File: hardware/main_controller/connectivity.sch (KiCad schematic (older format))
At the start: 16 parts

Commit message: Peripherals
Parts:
- removed JP?: Jumper, symbol Device:Jumper
- added J? (x2): Conn_01x08, symbol Connector_Generic:Conn_01x08
- added J? (x2): Conn_02x08_Odd_Even, symbol Connector_Generic:Conn_02x08_Odd_Even
- added J?: Conn_01x04, symbol Connector_Generic:Conn_01x04
- added J?: Conn_01x06, symbol Connector_Generic:Conn_01x06
- added J?: Conn_02x03_Counter_Clockwise, symbol Connector_Generic:Conn_02x03_Counter_Clockwise
- added J? (x2): RJ45, symbol Connector:RJ45
- added JP? (x3): Jumper_NO_Small, symbol Device:Jumper_NO_Small
- added R?: 4.7k, symbol Device:R
- added R?: 120, symbol Device:R
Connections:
- net labels added: CAN_H, CAN_L, CAN_PWR, CAN_RX, CAN_TX, GPIO_PE0, GPIO_PE1, GPIO_PE10, GPIO_PE11, GPIO_PE12, GPIO_PE13, GPIO_PE14, GPIO_PE15, GPIO_PE2, GPIO_PE3, GPIO_PE4, GPIO_PE5, GPIO_PE6, GPIO_PE7, GPIO_PE8, GPIO_PE9, I2C_SCL, I2C_SDA, SPI_CS1, SPI_CS2, SPI_CS3, SPI_MISO, SPI_MOSI, SPI_SCK
- wire segments 71 -> 219
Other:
- note added: "CAN"
- note added: "Deliver/Retrieve Power from CAN bus"
- note added: "GPIO"
- note added: "I2C"
- note added: "Optional CAN bus\ntermination resistor"
- note added: "SPI"
- moved on the sheet: C?, U?

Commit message: LEDs
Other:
- moved on the sheet: J?
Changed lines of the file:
@@
 L Connector_Generic:Conn_01x06 J?
 U 1 1 5FF94D26
-P 4650 4050
-F 0 "J?" H 4568 3525 50  0000 C CNN
-F 1 "Conn_01x06" H 4568 3616 50  0000 C CNN
-F 2 "" H 4650 4050 50  0001 C CNN
-F 3 "~" H 4650 4050 50  0001 C CNN
-	1    4650 4050
+P 4650 4200
+F 0 "J?" H 4568 3675 50  0000 C CNN
+F 1 "Conn_01x06" H 4568 3766 50  0000 C CNN
+F 2 "" H 4650 4200 50  0001 C CNN
+F 3 "~" H 4650 4200 50  0001 C CNN
+	1    4650 4200
 	-1   0    0    1
 $EndComp
 Wire Wire Line
-	4850 3750 4950 3750
-Wire Wire Line
-	4850 3850 4950 3850
-Wire Wire Line
-	4850 3950 4950 3950
-Wire Wire Line
-	4850 4050 4950 4050
-Wire Wire Line
-	4850 4150 4950 4150
-Wire Wire Line
-	4850 4250 4950 4250
-Text GLabel 4950 3750 2    50   Input ~ 0
+	4850 3900 4950 3900
+Wire Wire Line
+	4850 4000 4950 4000
+Wire Wire Line
+	4850 4100 4950 4100
+Wire Wire Line
+	4850 4200 4950 4200
+Wire Wire Line
+	4850 4300 4950 4300
+Wire Wire Line
+	4850 4400 4950 4400
+Text GLabel 4950 3900 2    50   Input ~ 0
 SPI_SCK
-Text GLabel 4950 3850 2    50   Input ~ 0
+Text GLabel 4950 4000 2    50   Input ~ 0
 SPI_MISO
-Text GLabel 4950 3950 2    50   Input ~ 0
+Text GLabel 4950 4100 2    50   Input ~ 0
 SPI_MOSI
-Text GLabel 4950 4050 2    50   Input ~ 0
+Text GLabel 4950 4200 2    50   Input ~ 0
 SPI_CS1
-Text GLabel 4950 4150 2    50   Input ~ 0
+Text GLabel 4950 4300 2    50   Input ~ 0
 SPI_CS2
-Text GLabel 4950 4250 2    50   Input ~ 0
+Text GLabel 4950 4400 2    50   Input ~ 0
 SPI_CS3
 $Comp
 L Connector_Generic:Conn_02x03_Counter_Clockwise J?
 U 1 1 5FFE4E2A
-P 4850 4900
-F 0 "J?" H 4900 5217 50  0000 C CNN
-F 1 "Conn_02x03_Counter_Clockwise" H 4900 5126 50  0000 C CNN
-F 2 "" H 4850 4900 50  0001 C CNN
-F 3 "~" H 4850 4900 50  0001 C CNN
-	1    4850 4900
+P 4850 5050
+F 0 "J?" H 4900 5367 50  0000 C CNN
+F 1 "Conn_02x03_Counter_Clockwise" H 4900 5276 50  0000 C CNN
+F 2 "" H 4850 5050 50  0001 C CNN
+F 3 "~" H 4850 5050 50  0001 C CNN
+	1    4850 5050
 	1    0    0    -1
 $EndComp
@@
 L power:+3V3 #PWR?
 U 1 1 5FFE6348
-P 4600 4650
-F 0 "#PWR?" H 4600 4500 50  0001 C CNN
-F 1 "+3V3" H 4615 4823 50  0000 C CNN
-F 2 "" H 4600 4650 50  0001 C CNN
-F 3 "" H 4600 4650 50  0001 C CNN
-	1    4600 4650
+P 4600 4800
+F 0 "#PWR?" H 4600 4650 50  0001 C CNN
+F 1 "+3V3" H 4615 4973 50  0000 C CNN
+F 2 "" H 4600 4800 50  0001 C CNN
+F 3 "" H 4600 4800 50  0001 C CNN
+	1    4600 4800
 	1    0    0    -1
 $EndComp
@@
 L power:GND #PWR?
 U 1 1 5FFE73F3
-P 5250 5150
-F 0 "#PWR?" H 5250 4900 50  0001 C CNN
-F 1 "GND" H 5255 4977 50  0000 C CNN
-F 2 "" H 5250 5150 50  0001 C CNN
-F 3 "" H 5250 5150 50  0001 C CNN
-	1    5250 5150
-	1    0    0    -1
-$EndComp
-Wire Wire Line
-	5150 4800 5250 4800
-Wire Wire Line
-	5250 4800 5250 4900
-Wire Wire Line
-	5150 4900 5250 4900
-Connection ~ 5250 4900
-Wire Wire Line
-	5250 4900 5250 5000
-Wire Wire Line
-	5250 5000 5150 5000
-Connection ~ 5250 5000
-Wire Wire Line
-	5250 5000 5250 5150
-Wire Wire Line
-	4650 4800 4600 4800
-Wire Wire Line
-	4600 4800 4600 4650
-Wire Wire Line
-	4650 5000 4600 5000
-Wire Wire Line
-	4600 5000 4600 4900
-Connection ~ 4600 4800
-Wire Wire Line
-	4650 4900 4600 4900
-Connection ~ 4600 4900
-Wire Wire Line
-	4600 4900 4600 4800
+P 5250 5300
+F 0 "#PWR?" H 5250 5050 50  0001 C CNN
+F 1 "GND" H 5255 5127 50  0000 C CNN
+F 2 "" H 5250 5300 50  0001 C CNN
+F 3 "" H 5250 5300 50  0001 C CNN
+	1    5250 5300
+	1    0    0    -1
+$EndComp
+Wire Wire Line
+	5150 4950 5250 4950
+Wire Wire Line
+	5250 4950 5250 5050
+Wire Wire Line
+	5150 5050 5250 5050
+Connection ~ 5250 5050
+Wire Wire Line
+	5250 5050 5250 5150
+Wire Wire Line
+	5250 5150 5150 5150
+Connection ~ 5250 5150
+Wire Wire Line
+	5250 5150 5250 5300
+Wire Wire Line
+	4650 4950 4600 4950
+Wire Wire Line
+	4600 4950 4600 4800
+Wire Wire Line
+	4650 5150 4600 5150
+Wire Wire Line
+	4600 5150 4600 5050
+Connection ~ 4600 4950
+Wire Wire Line
+	4650 5050 4600 5050
+Connection ~ 4600 5050
+Wire Wire Line
+	4600 5050 4600 4950
 Wire Notes Line
 	4150 3300 5700 3300
-Wire Notes Line
-	5700 3300 5700 5450
-Wire Notes Line
-	5700 5450 4150 5450
-Wire Notes Line
-	4150 5450 4150 3300
 Text Notes 4550 3500 2    129  ~ 0
 SPI
@@
 Text Notes 7250 3450 0    50   ~ 0
 Deliver/Retrieve Power from CAN bus
+Wire Notes Line
+	5700 5700 4150 5700
+Wire Notes Line
+	5700 3300 5700 5700
+Wire Notes Line
+	4150 3300 4150 5700
 $EndSCHEMATC

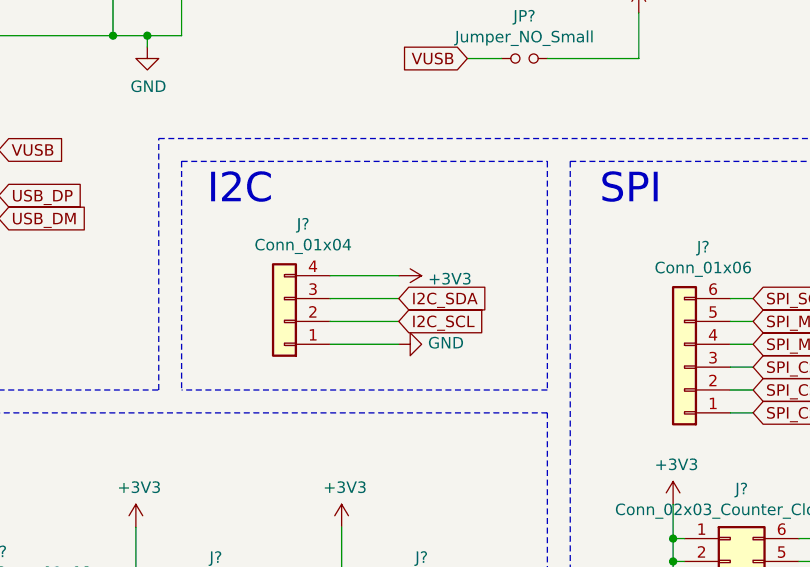
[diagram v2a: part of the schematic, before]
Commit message: MCU Supply and Oscillator
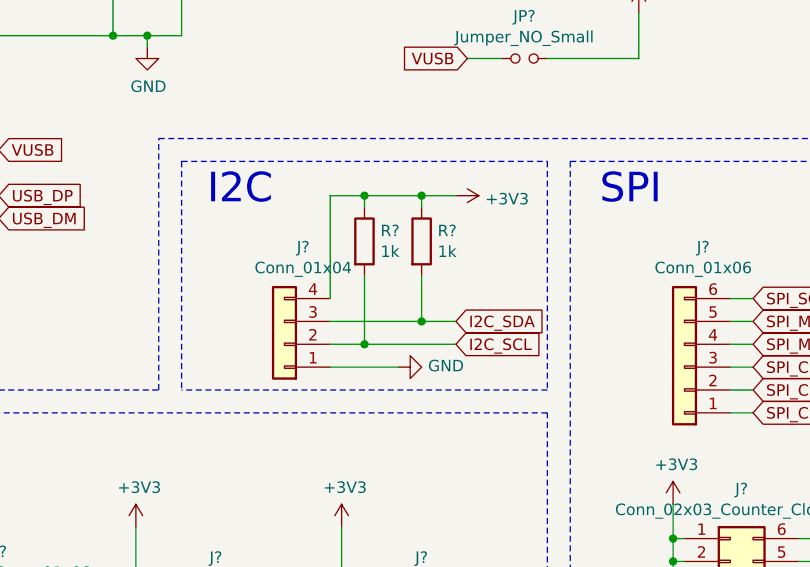
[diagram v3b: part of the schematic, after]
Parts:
- added R? (x2): 1k, symbol Device:R
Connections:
- net +3V3: now also R?.1, R?.1
- net I2C_SCL: now also R?.2
- net I2C_SDA: now also R?.2
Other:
- moved on the sheet: J?
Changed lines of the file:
@@
 L Connector_Generic:Conn_01x04 J?
 U 1 1 5FF49A2B
-P 2900 4000
-F 0 "J?" H 2818 3575 50  0000 C CNN
-F 1 "Conn_01x04" H 2818 3666 50  0000 C CNN
-F 2 "" H 2900 4000 50  0001 C CNN
-F 3 "~" H 2900 4000 50  0001 C CNN
-	1    2900 4000
+P 2900 4100
+F 0 "J?" H 2818 3675 50  0000 C CNN
+F 1 "Conn_01x04" H 2818 3766 50  0000 C CNN
+F 2 "" H 2900 4100 50  0001 C CNN
+F 3 "~" H 2900 4100 50  0001 C CNN
+	1    2900 4100
 	-1   0    0    1
 $EndComp
@@
 L power:GND #PWR?
 U 1 1 5FF4AF81
-P 3400 4100
-F 0 "#PWR?" H 3400 3850 50  0001 C CNN
-F 1 "GND" V 3405 3972 50  0000 R CNN
-F 2 "" H 3400 4100 50  0001 C CNN
-F 3 "" H 3400 4100 50  0001 C CNN
-	1    3400 4100
+P 3400 4200
+F 0 "#PWR?" H 3400 3950 50  0001 C CNN
+F 1 "GND" V 3405 4072 50  0000 R CNN
+F 2 "" H 3400 4200 50  0001 C CNN
+F 3 "" H 3400 4200 50  0001 C CNN
+	1    3400 4200
 	0    -1   -1   0
 $EndComp
-$Comp
-L power:+3V3 #PWR?
-U 1 1 5FF4C119
-P 3400 3800
-F 0 "#PWR?" H 3400 3650 50  0001 C CNN
-F 1 "+3V3" V 3415 3928 50  0000 L CNN
-F 2 "" H 3400 3800 50  0001 C CNN
-F 3 "" H 3400 3800 50  0001 C CNN
-	1    3400 3800
-	0    1    1    0
-$EndComp
-Wire Wire Line
-	3100 3800 3400 3800
-Wire Wire Line
-	3100 4100 3400 4100
-Wire Wire Line
-	3100 3900 3400 3900
-Wire Wire Line
-	3100 4000 3400 4000
-Text GLabel 3400 3900 2    50   Input ~ 0
+Wire Wire Line
+	3100 4200 3400 4200
+Text GLabel 3650 4000 2    50   Input ~ 0
 I2C_SDA
-Text GLabel 3400 4000 2    50   Input ~ 0
+Text GLabel 3650 4100 2    50   Input ~ 0
 I2C_SCL
 Wire Notes Line
@@
 Wire Notes Line
 	4150 3300 4150 5700
+$Comp
+L Device:R R?
+U 1 1 5FD1641F
+P 3250 3650
+F 0 "R?" H 3320 3696 50  0000 L CNN
+F 1 "1k" H 3320 3605 50  0000 L CNN
+F 2 "" V 3180 3650 50  0001 C CNN
+F 3 "~" H 3250 3650 50  0001 C CNN
+	1    3250 3650
+	1    0    0    -1
+$EndComp
+$Comp
+L Device:R R?
+U 1 1 5FD1719C
+P 3500 3650
+F 0 "R?" H 3570 3696 50  0000 L CNN
+F 1 "1k" H 3570 3605 50  0000 L CNN
+F 2 "" V 3430 3650 50  0001 C CNN
+F 3 "~" H 3500 3650 50  0001 C CNN
+	1    3500 3650
+	1    0    0    -1
+$EndComp
+Wire Wire Line
+	3100 4000 3500 4000
+Wire Wire Line
+	3100 4100 3250 4100
+$Comp
+L power:+3V3 #PWR?
+U 1 1 5FD4A956
+P 3650 3450
+F 0 "#PWR?" H 3650 3300 50  0001 C CNN
+F 1 "+3V3" V 3665 3578 50  0000 L CNN
+F 2 "" H 3650 3450 50  0001 C CNN
+F 3 "" H 3650 3450 50  0001 C CNN
+	1    3650 3450
+	0    1    1    0
+$EndComp
+Wire Wire Line
+	3650 3450 3500 3450
+Wire Wire Line
+	3250 3450 3250 3500
+Wire Wire Line
+	3500 3500 3500 3450
+Connection ~ 3500 3450
+Wire Wire Line
+	3500 3450 3250 3450
+Wire Wire Line
+	3250 3450 3100 3450
+Wire Wire Line
+	3100 3450 3100 3900
+Connection ~ 3250 3450
+Wire Wire Line
+	3250 3800 3250 4100
+Connection ~ 3250 4100
+Wire Wire Line
+	3250 4100 3650 4100
+Wire Wire Line
+	3500 3800 3500 4000
+Connection ~ 3500 4000
+Wire Wire Line
+	3500 4000 3650 4000
 $EndSCHEMATC

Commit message: Assigned names
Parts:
- gave numbers to parts that had none: 31

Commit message: usb protection
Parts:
- removed JP1: Jumper_NO_Small, symbol Device:Jumper_NO_Small
- added C19: 100nF, symbol Device:C
- added F1: 500mA, symbol Device:Polyfuse
- added JP1: JMP_USB_PWR, symbol Jumper:Jumper_3_Bridged12
- added JP4: JMP_USB_PU, symbol Device:Jumper_NO_Small
- added R24: 4.7k, symbol Device:R
- added R25: 10k, symbol Device:R
- added U4: USBLC6-2SC6, Package_TO_SOT_SMD:SOT-23-6, symbol Power_Protection:USBLC6-2SC6
- J10: value Conn_ARM_JTAG_SWD_20 -> JTAG_Connector
- J3: value Conn_01x08 -> GPIO_1
- J4: value Conn_01x08 -> GPIO_2
- J5: value Conn_02x08_Odd_Even -> GPIO_PWR_1
- J6: value Conn_01x04 -> I2C
- J7: value Conn_02x08_Odd_Even -> GPIO_PWR_2
- J8: value Conn_01x06 -> SPI
- J9: value Conn_02x03_Counter_Clockwise -> SPI_PWR
- JP2: value Jumper_NO_Small -> JMP_CAN_PWR
- JP3: value Jumper_NO_Small -> JMP_CAN_TERM
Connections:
- net +5V: now also F1.2
- net GND: now also C19.2, R25.1, U4.2 (GND)
- net STM_DP: now also JP4.2; no longer R7.2
- net USB_DM: now also U4.3 (I/O2); no longer J2.A7 (D-), J2.B7 (D-)
- net USB_DP: now also U4.1 (I/O1); no longer J2.A6 (D+), J2.B6 (D+)
- net VUSB: now also C19.1, JP1.2 (C), U4.5 (VBUS)
- new net: JP4.1, R7.2
- new net: F1.1, JP1.1 (A)
- new net: JP1.3 (B), R24.2
- new net DM: J2.A7 (D-), J2.B7 (D-), U4.4 (I/O2)
- new net DP: J2.A6 (D+), J2.B6 (D+), U4.6 (I/O1)
- new net VBUS_DETECT: R24.1, R25.2
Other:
- note added: "Jumper switches between bus-powered and self-powered device mode\n - Bridging 1-2 will power the device from the bus\n - Bridging 2-3 will not power the device from the bus. In this case,\n VBUS detection needs to be employed"
- note added: "USB DP pull-up resistor\nselect jumper"
- moved on the sheet: J1, J2, R1, R2, R5, R6, R7

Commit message: assigned footprints
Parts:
- C1, C19: footprint (none) -> Capacitor_SMD:C_0201_0603Metric
- F1: footprint (none) -> Fuse:Fuse_1206_3216Metric
- J1: footprint (none) -> Connector_USB:USB_Mini-B_Wuerth_65100516121_Horizontal
- J10: footprint (none) -> Connector_PinHeader_2.54mm:PinHeader_2x10_P2.54mm_Vertical
- J11, J12: footprint (none) -> Connector_RJ:RJ45_Wuerth_7499010001A_Horizontal
- J2: footprint (none) -> Connector_USB:USB_C_Receptacle_HRO_TYPE-C-31-M-12
- J3, J4: footprint (none) -> Connector_PinHeader_2.54mm:PinHeader_1x08_P2.54mm_Vertical
- J5, J7: footprint (none) -> Connector_PinHeader_2.54mm:PinHeader_2x08_P2.54mm_Vertical
- J6: footprint (none) -> Connector_PinHeader_2.54mm:PinHeader_1x04_P2.54mm_Vertical
- J8: footprint (none) -> Connector_PinHeader_2.54mm:PinHeader_1x06_P2.54mm_Vertical
- J9: footprint (none) -> Connector_PinHeader_2.54mm:PinHeader_2x03_P2.54mm_Vertical
- JP1: footprint (none) -> Connector_PinSocket_2.54mm:PinSocket_1x03_P2.54mm_Vertical
- JP2, JP3, JP4: footprint (none) -> Connector_PinSocket_2.54mm:PinSocket_1x02_P2.54mm_Vertical
- R1, R10, R11, R12, R13, R14, R2, R24, R25, R3, R4, R5, R6, R7, R8, R9: footprint (none) -> Resistor_SMD:R_0201_0603Metric
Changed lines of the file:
@@
 F 0 "J2" H 1207 2617 50  0000 C CNN
 F 1 "USB_C_Receptacle_USB2.0" H 1207 2526 50  0000 C CNN
-F 2 "" H 1250 1750 50  0001 C CNN
+F 2 "Connector_USB:USB_C_Receptacle_HRO_TYPE-C-31-M-12" H 1250 1750 50  0001 C CNN
 F 3 "https://www.usb.org/sites/default/files/documents/usb_type-c.zip" H 1250 1750 50  0001 C CNN
 	1    1100 1750
@@
 F 0 "J1" H 957 3917 50  0000 C CNN
 F 1 "USB_B_Mini" H 957 3826 50  0000 C CNN
-F 2 "" H 1050 3400 50  0001 C CNN
+F 2 "Connector_USB:USB_Mini-B_Wuerth_65100516121_Horizontal" H 1050 3400 50  0001 C CNN
 F 3 "~" H 1050 3400 50  0001 C CNN
 	1    900  3450
@@
 F 0 "R1" H 1870 2346 50  0000 L CNN
 F 1 "5.1k" H 1870 2255 50  0000 L CNN
-F 2 "" V 1730 2300 50  0001 C CNN
+F 2 "Resistor_SMD:R_0201_0603Metric" V 1730 2300 50  0001 C CNN
 F 3 "~" H 1800 2300 50  0001 C CNN
 	1    1800 2300
@@
 F 0 "R2" H 2170 2346 50  0000 L CNN
 F 1 "5.1k" H 2170 2255 50  0000 L CNN
-F 2 "" V 2030 2300 50  0001 C CNN
+F 2 "Resistor_SMD:R_0201_0603Metric" V 2030 2300 50  0001 C CNN
 F 3 "~" H 2100 2300 50  0001 C CNN
 	1    2100 2300
@@
 F 0 "R5" V 4393 1700 50  0000 C CNN
 F 1 "22" V 4484 1700 50  0000 C CNN
-F 2 "" V 4530 1700 50  0001 C CNN
+F 2 "Resistor_SMD:R_0201_0603Metric" V 4530 1700 50  0001 C CNN
 F 3 "~" H 4600 1700 50  0001 C CNN
 	1    4600 1700
@@
 F 0 "R6" V 4393 2000 50  0000 C CNN
 F 1 "22" V 4484 2000 50  0000 C CNN
-F 2 "" V 4530 2000 50  0001 C CNN
+F 2 "Resistor_SMD:R_0201_0603Metric" V 4530 2000 50  0001 C CNN
 F 3 "~" H 4600 2000 50  0001 C CNN
 	1    4600 2000
@@
 F 0 "R7" H 4920 1196 50  0000 L CNN
 F 1 "1.5k" H 4920 1105 50  0000 L CNN
-F 2 "" V 4780 1150 50  0001 C CNN
+F 2 "Resistor_SMD:R_0201_0603Metric" V 4780 1150 50  0001 C CNN
 F 3 "~" H 4850 1150 50  0001 C CNN
 	1    4850 1150
@@
 F 0 "J10" H 6821 1946 50  0000 R CNN
 F 1 "JTAG_Connector" H 6821 1855 50  0000 R CNN
-F 2 "" H 7800 850 50  0001 L TNN
+F 2 "Connector_PinHeader_2.54mm:PinHeader_2x10_P2.54mm_Vertical" H 7800 850 50  0001 L TNN
 F 3 "http://infocenter.arm.com/help/topic/com.arm.doc.dui0499b/DUI0499B_system_design_reference.pdf" V 7000 650 50  0001 C CNN
 	1    7350 1900
@@
 F 0 "C1" H 6565 1346 50  0000 L CNN
 F 1 "100nF" H 6565 1255 50  0000 L CNN
-F 2 "" H 6488 1150 50  0001 C CNN
+F 2 "Capacitor_SMD:C_0201_0603Metric" H 6488 1150 50  0001 C CNN
 F 3 "~" H 6450 1300 50  0001 C CNN
 	1    6450 1300
@@
 F 0 "R9" H 8270 1196 50  0000 L CNN
 F 1 "10k" H 8270 1105 50  0000 L CNN
-F 2 "" V 8130 1150 50  0001 C CNN
+F 2 "Resistor_SMD:R_0201_0603Metric" V 8130 1150 50  0001 C CNN
 F 3 "~" H 8200 1150 50  0001 C CNN
 	1    8200 1150
@@
 F 0 "R12" H 8570 1196 50  0000 L CNN
 F 1 "10k" H 8570 1105 50  0000 L CNN
-F 2 "" V 8430 1150 50  0001 C CNN
+F 2 "Resistor_SMD:R_0201_0603Metric" V 8430 1150 50  0001 C CNN
 F 3 "~" H 8500 1150 50  0001 C CNN
 	1    8500 1150
@@
 F 0 "R13" H 8870 1196 50  0000 L CNN
 F 1 "10k" H 8870 1105 50  0000 L CNN
-F 2 "" V 8730 1150 50  0001 C CNN
+F 2 "Resistor_SMD:R_0201_0603Metric" V 8730 1150 50  0001 C CNN
 F 3 "~" H 8800 1150 50  0001 C CNN
 	1    8800 1150
@@
 F 0 "R14" H 9170 1196 50  0000 L CNN
 F 1 "10k" H 9170 1105 50  0000 L CNN
-F 2 "" V 9030 1150 50  0001 C CNN
+F 2 "Resistor_SMD:R_0201_0603Metric" V 9030 1150 50  0001 C CNN
 F 3 "~" H 9100 1150 50  0001 C CNN
 	1    9100 1150
@@
 F 0 "R10" H 8270 2396 50  0000 L CNN
 F 1 "10k" H 8270 2305 50  0000 L CNN
-F 2 "" V 8130 2350 50  0001 C CNN
+F 2 "Resistor_SMD:R_0201_0603Metric" V 8130 2350 50  0001 C CNN
 F 3 "~" H 8200 2350 50  0001 C CNN
 	1    8200 2350
@@
 F 0 "R8" H 6570 5046 50  0000 L CNN
 F 1 "4.7k" H 6570 4955 50  0000 L CNN
-F 2 "" V 6430 5000 50  0001 C CNN
+F 2 "Resistor_SMD:R_0201_0603Metric" V 6430 5000 50  0001 C CNN
 F 3 "~" H 6500 5000 50  0001 C CNN
 	1    6500 5000
@@
 F 0 "R11" H 8270 4746 50  0000 L CNN
 F 1 "120" H 8270 4655 50  0000 L CNN
-F 2 "" V 8130 4700 50  0001 C CNN
+F 2 "Resistor_SMD:R_0201_0603Metric" V 8130 4700 50  0001 C CNN
 F 3 "~" H 8200 4700 50  0001 C CNN
 	1    8200 4700
@@
 F 0 "JP3" V 8154 4398 50  0000 L CNN
 F 1 "JMP_CAN_TERM" V 8245 4398 50  0000 L CNN
-F 2 "" H 8200 4350 50  0001 C CNN
+F 2 "Connector_PinSocket_2.54mm:PinSocket_1x02_P2.54mm_Vertical" H 8200 4350 50  0001 C CNN
 F 3 "~" H 8200 4350 50  0001 C CNN
 	1    8200 4350
@@
 F 0 "J3" H 1630 4992 50  0000 L CNN
 F 1 "GPIO_1" H 1630 4901 50  0000 L CNN
-F 2 "" H 1550 5000 50  0001 C CNN
+F 2 "Connector_PinHeader_2.54mm:PinHeader_1x08_P2.54mm_Vertical" H 1550 5000 50  0001 C CNN
 F 3 "~" H 1550 5000 50  0001 C CNN
 	1    1550 5000
@@
 F 0 "J4" H 1630 5992 50  0000 L CNN
 F 1 "GPIO_2" H 1630 5901 50  0000 L CNN
-F 2 "" H 1550 6000 50  0001 C CNN
+F 2 "Connector_PinHeader_2.54mm:PinHeader_1x08_P2.54mm_Vertical" H 1550 6000 50  0001 C CNN
 F 3 "~" H 1550 6000 50  0001 C CNN
 	1    1550 6000
@@
 F 0 "J5" H 2600 6067 50  0000 C CNN
 F 1 "GPIO_PWR_1" H 2600 5976 50  0000 C CNN
-F 2 "" H 2550 5550 50  0001 C CNN
+F 2 "Connector_PinHeader_2.54mm:PinHeader_2x08_P2.54mm_Vertical" H 2550 5550 50  0001 C CNN
 F 3 "~" H 2550 5550 50  0001 C CNN
 	1    2550 5550
@@
 F 0 "J7" H 3500 6067 50  0000 C CNN
 F 1 "GPIO_PWR_2" H 3500 5976 50  0000 C CNN
-F 2 "" H 3450 5550 50  0001 C CNN
+F 2 "Connector_PinHeader_2.54mm:PinHeader_2x08_P2.54mm_Vertical" H 3450 5550 50  0001 C CNN
 F 3 "~" H 3450 5550 50  0001 C CNN
 	1    3450 5550
@@
 F 0 "J6" H 2818 3675 50  0000 C CNN
 F 1 "I2C" H 2818 3766 50  0000 C CNN
-F 2 "" H 2900 4100 50  0001 C CNN
+F 2 "Connector_PinHeader_2.54mm:PinHeader_1x04_P2.54mm_Vertical" H 2900 4100 50  0001 C CNN
 F 3 "~" H 2900 4100 50  0001 C CNN
 	1    2900 4100
@@
 F 0 "J8" H 4568 3675 50  0000 C CNN
 F 1 "SPI" H 4568 3766 50  0000 C CNN
-F 2 "" H 4650 4200 50  0001 C CNN
+F 2 "Connector_PinHeader_2.54mm:PinHeader_1x06_P2.54mm_Vertical" H 4650 4200 50  0001 C CNN
 F 3 "~" H 4650 4200 50  0001 C CNN
 	1    4650 4200
@@
 F 0 "J9" H 4900 5367 50  0000 C CNN
 F 1 "SPI_PWR" H 4900 5276 50  0000 C CNN
-F 2 "" H 4850 5050 50  0001 C CNN
+F 2 "Connector_PinHeader_2.54mm:PinHeader_2x03_P2.54mm_Vertical" H 4850 5050 50  0001 C CNN
 F 3 "~" H 4850 5050 50  0001 C CNN
 	1    4850 5050
@@
 F 0 "J11" H 9220 3854 50  0000 R CNN
 F 1 "RJ45" H 9220 3945 50  0000 R CNN
-F 2 "" V 9550 3875 50  0001 C CNN
+F 2 "Connector_RJ:RJ45_Wuerth_7499010001A_Horizontal" V 9550 3875 50  0001 C CNN
 F 3 "~" V 9550 3875 50  0001 C CNN
 	1    9550 3850
@@
 F 0 "J12" H 9220 4954 50  0000 R CNN
 F 1 "RJ45" H 9220 5045 50  0000 R CNN
-F 2 "" V 9550 4975 50  0001 C CNN
+F 2 "Connector_RJ:RJ45_Wuerth_7499010001A_Horizontal" V 9550 4975 50  0001 C CNN
 F 3 "~" V 9550 4975 50  0001 C CNN
 	1    9550 4950
@@
 F 0 "JP2" H 7600 3885 50  0000 C CNN
 F 1 "JMP_CAN_PWR" H 7600 3794 50  0000 C CNN
-F 2 "" H 7600 3700 50  0001 C CNN
+F 2 "Connector_PinSocket_2.54mm:PinSocket_1x02_P2.54mm_Vertical" H 7600 3700 50  0001 C CNN
 F 3 "~" H 7600 3700 50  0001 C CNN
 	1    7600 3700
@@
 F 0 "R3" H 3320 3696 50  0000 L CNN
 F 1 "1k" H 3320 3605 50  0000 L CNN
-F 2 "" V 3180 3650 50  0001 C CNN
+F 2 "Resistor_SMD:R_0201_0603Metric" V 3180 3650 50  0001 C CNN
 F 3 "~" H 3250 3650 50  0001 C CNN
 	1    3250 3650
@@
 F 0 "R4" H 3570 3696 50  0000 L CNN
 F 1 "1k" H 3570 3605 50  0000 L CNN
-F 2 "" V 3430 3650 50  0001 C CNN
+F 2 "Resistor_SMD:R_0201_0603Metric" V 3430 3650 50  0001 C CNN
 F 3 "~" H 3500 3650 50  0001 C CNN
 	1    3500 3650
@@
 F 0 "R24" V 3993 3100 50  0000 C CNN
 F 1 "4.7k" V 4084 3100 50  0000 C CNN
-F 2 "" V 4130 3100 50  0001 C CNN
+F 2 "Resistor_SMD:R_0201_0603Metric" V 4130 3100 50  0001 C CNN
 F 3 "~" H 4200 3100 50  0001 C CNN
 	1    4200 3100
@@
 F 0 "R25" V 4493 3100 50  0000 C CNN
 F 1 "10k" V 4584 3100 50  0000 C CNN
-F 2 "" V 4630 3100 50  0001 C CNN
+F 2 "Resistor_SMD:R_0201_0603Metric" V 4630 3100 50  0001 C CNN
 F 3 "~" H 4700 3100 50  0001 C CNN
 	1    4700 3100
@@
 F 0 "JP4" V 4804 1498 50  0000 L CNN
 F 1 "JMP_USB_PU" V 4895 1498 50  0000 L CNN
-F 2 "" H 4850 1450 50  0001 C CNN
+F 2 "Connector_PinSocket_2.54mm:PinSocket_1x02_P2.54mm_Vertical" H 4850 1450 50  0001 C CNN
 F 3 "~" H 4850 1450 50  0001 C CNN
 	1    4850 1450
@@
 F 0 "C19" H 2250 1900 50  0000 L CNN
 F 1 "100nF" H 2250 1800 50  0000 L CNN
-F 2 "" H 2538 1750 50  0001 C CNN
+F 2 "Capacitor_SMD:C_0201_0603Metric" H 2538 1750 50  0001 C CNN
 F 3 "~" H 2500 1900 50  0001 C CNN
 	1    2500 1900
@@
 F 0 "JP1" V 3904 2767 50  0000 L CNN
 F 1 "JMP_USB_PWR" V 3995 2767 50  0000 L CNN
-F 2 "" H 3950 2700 50  0001 C CNN
+F 2 "Connector_PinSocket_2.54mm:PinSocket_1x03_P2.54mm_Vertical" H 3950 2700 50  0001 C CNN
 F 3 "~" H 3950 2700 50  0001 C CNN
 	1    3950 2700
@@
 F 0 "F1" V 3475 2400 50  0000 C CNN
 F 1 "500mA" V 3566 2400 50  0000 C CNN
-F 2 "" H 3750 2200 50  0001 L CNN
+F 2 "Fuse:Fuse_1206_3216Metric" H 3750 2200 50  0001 L CNN
 F 3 "~" H 3700 2400 50  0001 C CNN
 	1    3700 2400
